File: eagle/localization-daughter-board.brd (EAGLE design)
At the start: 65 x 30 mm, 7 parts, among them U1 LM340MP-5.0/NOPB, U2 STM32F042FXP

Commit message: Just saving progress
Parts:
- added J2: (no value), SparkFun-Connectors:JST-5-PTH-VERT
- added J3: (no value), Localization-Daughter-Board:MOLEX-053253-0370
- added U3: SN65HVD256DR, Localization-Daughter-Board:D8
- added U4: TXS0101DCKR, Localization-Daughter-Board:DCK6
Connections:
- new net DYN_OE: U4.5
- new net N$2: J2.2, U3.7
- new net N$3: J2.3, U3.6
- new net UART_DYN_3V3: U4.3
- new net UART_DYN_5V: J3.3, U4.4
- net +12V: now also J2.5
- net +3V3: now also U3.5, U4.1
- net +5V: now also J2.1, U3.3, U4.6
- net CAN_RX: now also U3.4
- net CAN_TX: now also U3.1
- net GND: now also J2.4, J3.1, U3.2, U4.2
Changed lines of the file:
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@@
 </element>
 <element name="J1" library="SparkFun-Connectors" package="1X05" value="" x="10.16" y="13.97" rot="R270"/>
+<element name="J2" library="SparkFun-Connectors" package="JST-5-PTH-VERT" value="" x="52.07" y="17.78"/>
+<element name="U3" library="Localization-Daughter-Board" library_urn="urn:adsk.eagle:library:1230207" package="D8" value="SN65HVD256DR" x="35.56" y="7.62">
+<attribute name="MANUFACTURER_PART_NUMBER" value="SN65HVD256DR" x="35.56" y="7.62" size="1.778" layer="27" display="off"/>
+<attribute name="VENDOR" value="Texas Instruments" x="35.56" y="7.62" size="1.778" layer="27" display="off"/>
+</element>
+<element name="J3" library="Localization-Daughter-Board" library_urn="urn:adsk.eagle:library:1230207" package="MOLEX-053253-0370" value="" x="48.26" y="8.89"/>
+<element name="U4" library="Localization-Daughter-Board" library_urn="urn:adsk.eagle:library:1230207" package="DCK6" package3d_urn="urn:adsk.eagle:package:1230550/1" value="TXS0101DCKR" x="49.53" y="5.08">
+<attribute name="MANUFACTURER_PART_NUMBER" value="TXS0101DCKR" x="49.53" y="5.08" size="1.778" layer="27" display="off"/>
+<attribute name="VENDOR" value="Texas Instruments" x="49.53" y="5.08" size="1.778" layer="27" display="off"/>
+</element>
 </elements>
 <signals>
@@
 <contactref element="C1" pad="2"/>
 <contactref element="J1" pad="2"/>
+<contactref element="U3" pad="2"/>
+<contactref element="J3" pad="1"/>
+<contactref element="U4" pad="2"/>
+<contactref element="J2" pad="4"/>
+<wire x1="50.26" y1="11.04" x2="54.07" y2="17.96" width="0" layer="19" extent="1-1"/>
 </signal>
 <signal name="+12V">
 <contactref element="U1" pad="1"/>
+<contactref element="J2" pad="5"/>
+<wire x1="21.35" y1="22.2504" x2="56.07" y2="17.96" width="0" layer="19" extent="1-1"/>
 </signal>
 <signal name="+5V">
@@
 <vertex x="0.52" y="3.17"/>
 </polygon>
+<contactref element="U3" pad="3"/>
+<contactref element="U4" pad="6"/>
+<contactref element="J2" pad="1"/>
+<wire x1="50.5079" y1="5.73" x2="48.07" y2="17.96" width="0" layer="19" extent="1-1"/>
+<wire x1="33.0962" y1="6.985" x2="50.5079" y2="5.73" width="0" layer="19" extent="1-1"/>
+<wire x1="16.75" y1="22.2504" x2="33.0962" y2="6.985" width="0" layer="19" extent="1-1"/>
 <wire x1="11.43" y1="27.94" x2="16.75" y2="22.2504" width="0" layer="19" extent="1-1"/>
 </signal>
@@
 <contactref element="U$1" pad="1"/>
 <contactref element="J1" pad="1"/>
-<wire x1="10.16" y1="13.97" x2="8.89" y2="25.4" width="0" layer="19" extent="1-1"/>
+<contactref element="U3" pad="5"/>
+<contactref element="U4" pad="1"/>
+<wire x1="38.0238" y1="5.715" x2="48.5521" y2="5.73" width="0" layer="19" extent="1-1"/>
+<wire x1="10.16" y1="13.97" x2="38.0238" y2="5.715" width="0" layer="19" extent="1-1"/>
+<wire x1="8.89" y1="25.4" x2="10.16" y2="13.97" width="0" layer="19" extent="1-1"/>
 </signal>
 <signal name="3V3">
@@
 <signal name="CAN_TX">
 <contactref element="U2" pad="18"/>
+<contactref element="U3" pad="1"/>
+<wire x1="19.404996875" y1="4.699" x2="33.0962" y2="9.525" width="0" layer="19" extent="1-1"/>
 </signal>
 <signal name="CAN_RX">
 <contactref element="U2" pad="17"/>
+<contactref element="U3" pad="4"/>
+<wire x1="18.755" y1="4.699" x2="33.0962" y2="5.715" width="0" layer="19" extent="1-1"/>
 </signal>
 <signal name="SDA1">
@@
 <contactref element="U2" pad="8"/>
 </signal>
+<signal name="N$2">
+<contactref element="J2" pad="2"/>
+<contactref element="U3" pad="7"/>
+<wire x1="38.0238" y1="8.255" x2="50.07" y2="17.96" width="0" layer="19" extent="1-1"/>
+</signal>
+<signal name="N$3">
+<contactref element="J2" pad="3"/>
+<contactref element="U3" pad="6"/>
+<wire x1="38.0238" y1="6.985" x2="52.07" y2="17.96" width="0" layer="19" extent="1-1"/>
+</signal>
+<signal name="UART_DYN_5V">
+<contactref element="J3" pad="3"/>
+<contactref element="U4" pad="4"/>
+<wire x1="50.5079" y1="4.43" x2="54.26" y2="11.04" width="0" layer="19" extent="1-1"/>
+</signal>
+<signal name="DYN_OE">
+<contactref element="U4" pad="5"/>
+</signal>
+<signal name="UART_DYN_3V3">
+<contactref element="U4" pad="3"/>
+</signal>
 </signals>

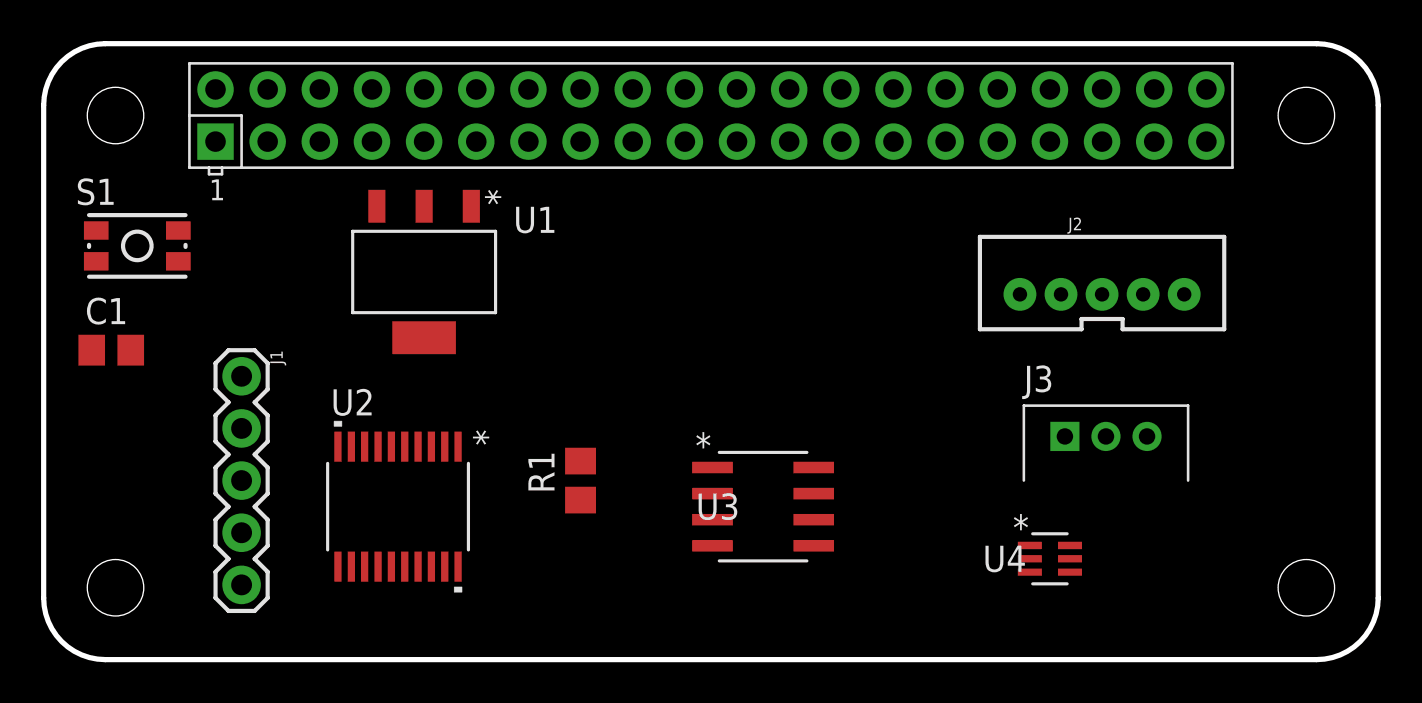
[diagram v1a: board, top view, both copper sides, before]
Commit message: Finished initial schematic
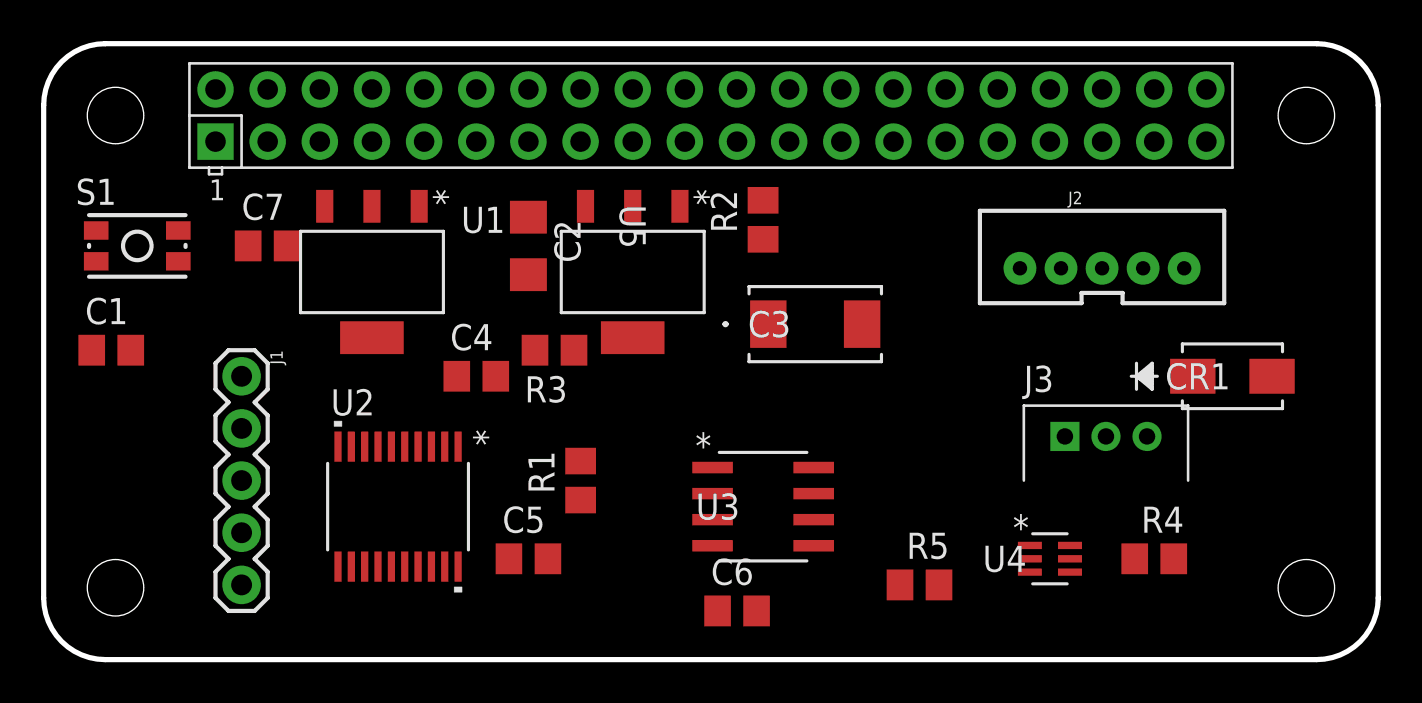
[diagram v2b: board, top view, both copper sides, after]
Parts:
- added C2: 10u, resistor:C1206
- added C3: 100u, Localization-Daughter-Board:F93-C
- added C4, C5, C6: 22u, resistor:C0805
- added C7: 0.1u, resistor:C0805
- added CR1: STPS2H100A, Localization-Daughter-Board:SMA
- added R2, R3: (no value), resistor:R0805
- added R4, R5: 10k, resistor:R0805
- added U5: LMS8117AMP-ADJ/NOPB, Localization-Daughter-Board:MP04A
- moved U1 2.54 mm to (16.5, 19.1)
- moved J2 1.27 mm to (52.1, 19.1)
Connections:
- new net +7V4: C3.1, J3.2, R2.2, U5.2, U5.4
- new net N$4: R2.1, R3.1, U5.1
- new net N$5: CR1.2, J2.5
- net +12V: now also C2.1, C4.1, C5.1, CR1.1, U5.3; no longer J2.5
- net +3V3: now also R5.2, U$1.17
- net +5V: now also C6.1, C7.1, R4.2
- net DYN_OE: now also R5.1
- net GND: now also C2.2, C3.2, C4.2, C5.2, C6.2, C7.2, R3.2
- net UART_DYN_5V: now also R4.1

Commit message: Fixed dynamixel connections
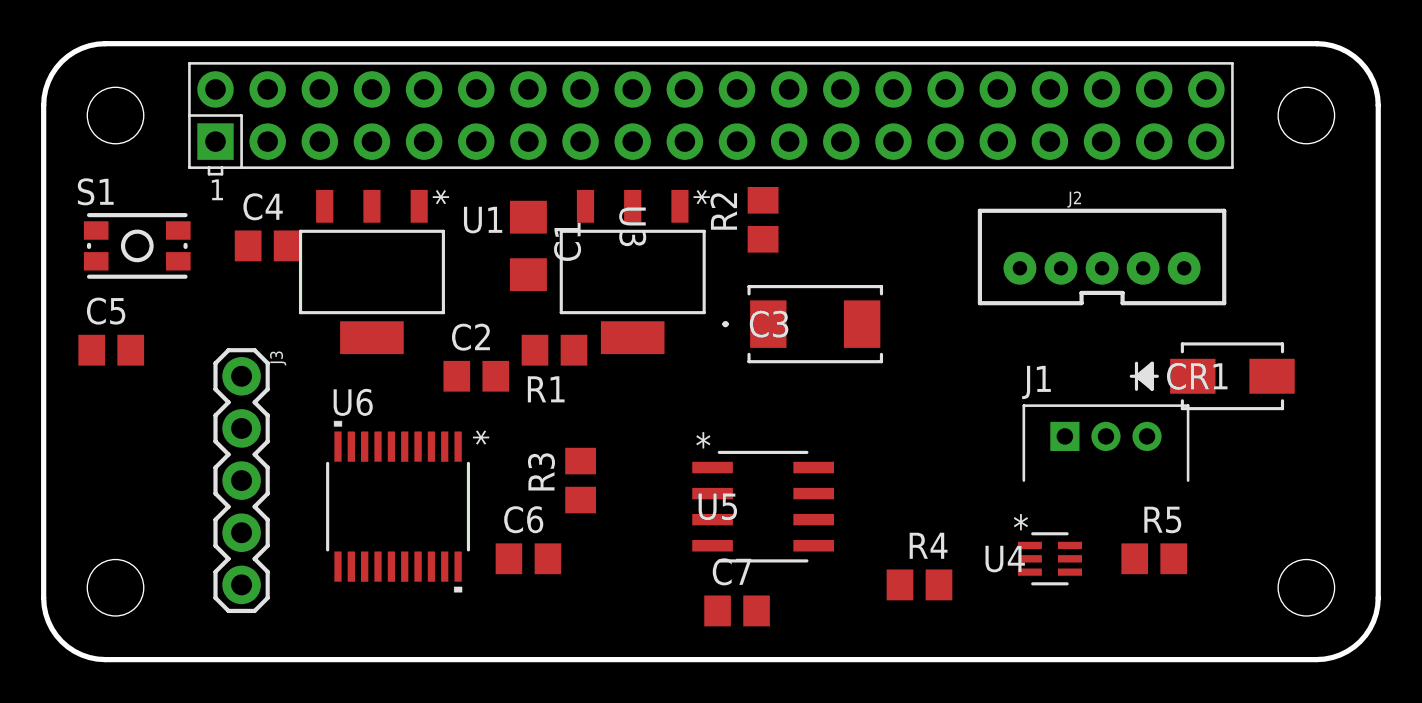
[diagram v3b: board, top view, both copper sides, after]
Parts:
- removed U$1: RPI-ZERO, RPI-Zero:RASPBERRYPI_BASTELSTUBE_V13_RASPI_BOARD_B+_FULL
- added U6: STM32F042FXP, Localization-Daughter-Board:TSSOP20
- C1: value 100nF -> 10u; device resistor:C0805 -> resistor:C1206
- C2: value 10u -> 22u; device resistor:C1206 -> resistor:C0805
- C4: value 22u -> 0.1u
- C5: value 22u -> 100nF
- C7: value 0.1u -> 22u
- J1: device SparkFun-Connectors:1X05 -> Localization-Daughter-Board:MOLEX-053253-0370
- J3: device Localization-Daughter-Board:MOLEX-053253-0370 -> SparkFun-Connectors:1X05
- R1: value 10k -> (none)
- R3: value (none) -> 10k
- U2: value STM32F042FXP -> RPI-ZERO; device Localization-Daughter-Board:TSSOP20 -> RPI-Zero:RASPBERRYPI_BASTELSTUBE_V13_RASPI_BOARD_B+_FULL
- U3: value SN65HVD256DR -> LMS8117AMP-ADJ/NOPB; device Localization-Daughter-Board:D8 -> Localization-Daughter-Board:MP04A
- U5: value LMS8117AMP-ADJ/NOPB -> SN65HVD256DR; device Localization-Daughter-Board:MP04A -> Localization-Daughter-Board:D8
- moved J1 38.4 mm to (48.3, 8.89), turned to 0 degrees
- moved J3 38.4 mm to (10.2, 14.0), turned to 270 degrees
- moved C7 29.0 mm to (34.3, 2.54)
- moved C5 22.7 mm to (3.81, 15.2)
- moved C1 20.9 mm to (24.1, 20.3), turned to 270 degrees
- moved U2 18.8 mm to (0.52, 0.17), turned to 0 degrees
- moved U3 13.1 mm to (29.2, 19.1), turned to 270 degrees
- moved U5 13.1 mm to (35.6, 7.62), turned to 0 degrees
- moved C4 12.0 mm to (11.4, 20.3)
- moved R4 11.5 mm to (43.2, 3.81)
- moved R5 11.5 mm to (54.6, 5.08)
- moved C6 10.5 mm to (24.1, 5.08)
- moved C2 6.84 mm to (21.6, 14.0), turned to 0 degrees
- moved R1 6.48 mm to (25.4, 15.2), turned to 180 degrees
- moved R3 6.48 mm to (26.7, 8.89), turned to 90 degrees
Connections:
- removed net UART_DYN: U2.8
- net +12V: now also C1.1, C6.1, U3.3; no longer C4.1, C5.1, U5.3
- net +3V3: now also J3.1, R4.2, U2.1, U2.17, U5.5; no longer J1.1, R5.2, U$1.1, U$1.17, U3.5
- net +5V: now also C4.1, R5.2, U2.2, U2.4, U5.3; no longer C6.1, R4.2, U$1.2, U$1.4, U3.3
- net +7V4: now also J1.2, U3.2, U3.4; no longer J3.2, U5.2, U5.4
- net 3V3: now also U6.16, U6.5; no longer U2.16, U2.5
- net CAN_RX: now also U5.4, U6.17; no longer U2.17, U3.4
- net CAN_TX: now also U5.1, U6.18; no longer U2.18, U3.1
- net DYN_OE: now also R4.1; no longer R5.1
- net GND: now also J1.1, J3.2, R1.2, R3.1, U2.14, U2.20, U2.25, U2.30, U2.34, U2.39, U2.6, U2.9, U5.2, U6.15; no longer J1.2, J3.1, R1.1, R3.2, U$1.14, U$1.20, U$1.25, U$1.30, U$1.34, U$1.39, U$1.6, U$1.9, U2.15, U3.2
- net N$1: now also R3.2, U6.1; no longer R1.2, U2.1
- net N$2: now also U5.7; no longer U3.7
- net N$3: now also U5.6; no longer U3.6
- net N$4: now also R1.1, U3.1; no longer R3.1, U5.1
- net NRST: now also C5.1, J3.5, U6.4; no longer C1.1, J1.5, U2.4
- net SCL1: now also U2.5, U6.3; no longer U$1.5, U2.3
- net SDA1: now also U2.3, U6.2; no longer U$1.3, U2.2
- net SWCLK: now also J3.4, U6.20; no longer J1.4, U2.20
- net SWDIO: now also J3.3, U6.19; no longer J1.3, U2.19
- net UART_DYN_3V3: now also U6.8
- net UART_DYN_5V: now also J1.3, R5.1; no longer J3.3, R4.1

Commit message: Finished initial power layout
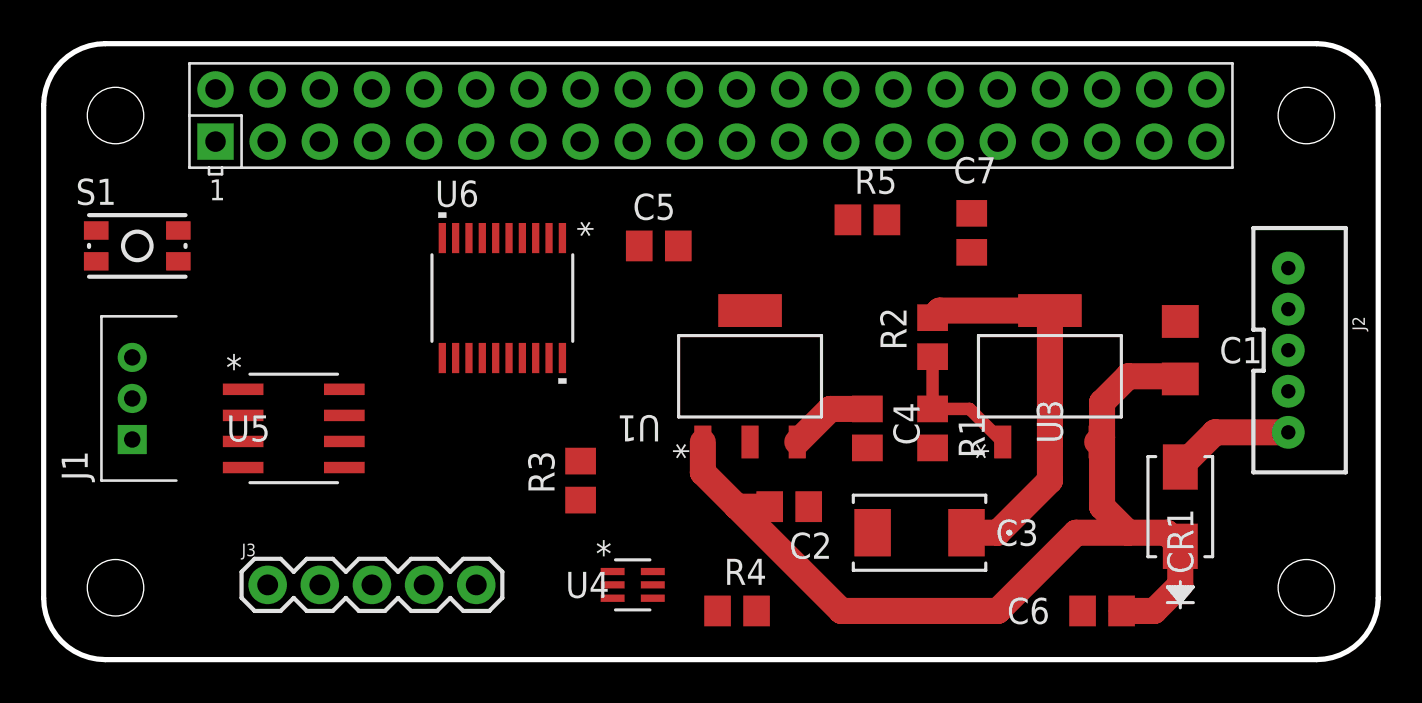
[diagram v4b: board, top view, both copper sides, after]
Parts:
- moved J1 41.3 mm to (6.99, 8.89), turned to 90 degrees
- moved C1 32.2 mm to (55.9, 15.2), turned to 90 degrees
- moved C4 30.5 mm to (40.6, 11.4), turned to 270 degrees
- moved C6 28.1 mm to (52.1, 2.54), turned to 180 degrees
- moved C5 27.1 mm to (30.5, 20.3)
- moved U5 23.2 mm to (12.7, 11.4)
- moved C7 21.7 mm to (45.7, 21.0), turned to 90 degrees
- moved R5 21.6 mm to (40.6, 21.6)
- moved U3 20.9 mm to (49.5, 14.0), turned to 90 degrees
- moved U4 20.4 mm to (29.2, 3.81)
- moved U1 19.1 mm to (34.9, 14.0), turned to 90 degrees
- moved R1 18.8 mm to (43.8, 11.4), turned to 270 degrees
- moved C2 16.5 mm to (36.8, 7.62)
- moved C3 11.4 mm to (43.2, 6.35), turned to 180 degrees
- moved U6 11.4 mm to (22.9, 17.8)
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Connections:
- net N$5 renamed VIN
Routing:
- net +12V: track 0.00 -> 47.8 mm
- net +7V4: track 0.00 -> 19.3 mm
- net N$4: track 0.00 -> 6.63 mm
- net VIN: track 0.00 -> 5.96 mm
- net +5V: track 0.00 -> 4.08 mm
- added copper zone on layer 16, net +3V3
- removed copper zone on layer 16, net +5V

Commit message: Finished initial design
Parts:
- moved U5 42.2 mm to (54.6, 16.5)
- moved R5 33.3 mm to (8.89, 11.4), turned to 270 degrees
- moved R4 24.1 mm to (10.2, 2.54)
- moved C5 20.4 mm to (10.2, 21.6), turned to 90 degrees
- moved U4 19.4 mm to (10.2, 7.62), turned to 90 degrees
- moved R3 18.0 mm to (14.0, 21.6), turned to 270 degrees
- moved C1 8.26 mm to (47.6, 15.2)
- moved CR1 7.62 mm to (48.3, 7.62)
- moved U3 7.62 mm to (41.9, 14.0)
- moved C2 7.62 mm to (29.2, 7.62)
- moved C3 7.62 mm to (35.6, 6.35)
- moved C4 7.62 mm to (33.0, 11.4)
- moved C6 7.62 mm to (44.5, 2.54)
- moved R1 7.62 mm to (36.2, 11.4)
- moved R2 7.62 mm to (36.2, 15.9)
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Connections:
- removed net 3V3: U6.16, U6.5
- net +3V3: now also U6.16, U6.5
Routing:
- net +5V: track 4.08 -> 123.1 mm, vias 0 -> 3
- net CAN_RX: track 0.00 -> 41.5 mm
- net CAN_TX: track 0.00 -> 39.4 mm
- net +7V4: track 19.3 -> 55.0 mm, vias 0 -> 1
- net NRST: track 0.00 -> 35.1 mm
- net SWCLK: track 0.00 -> 20.3 mm
- net +3V3: track 0.00 -> 17.9 mm, vias 0 -> 3
- net SWDIO: track 0.00 -> 14.1 mm
- net UART_DYN_5V: track 0.00 -> 13.8 mm
- net SCL1: track 0.00 -> 12.3 mm
- net SDA1: track 0.00 -> 10.8 mm
- net DYN_OE: track 0.00 -> 7.73 mm
- net VIN: track 5.96 -> 13.6 mm
- net UART_DYN_3V3: track 0.00 -> 7.58 mm
- net N$3: track 0.00 -> 4.33 mm
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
